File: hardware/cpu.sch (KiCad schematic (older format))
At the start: 76 parts, among them J801 HANDSFREE, J802 microphone, J803 HEADPHONES, P801 TX_SW_WIRE, Q801 Q_PMOS_DGS, SW801 SW_PUSH, SW802 SW, SW803 SW, SW804 SW, SW805 SW, SW806 SW, SW807 SW, SW808 encoder, SW809 encoder, U801 STM32F401, U802 WM8731

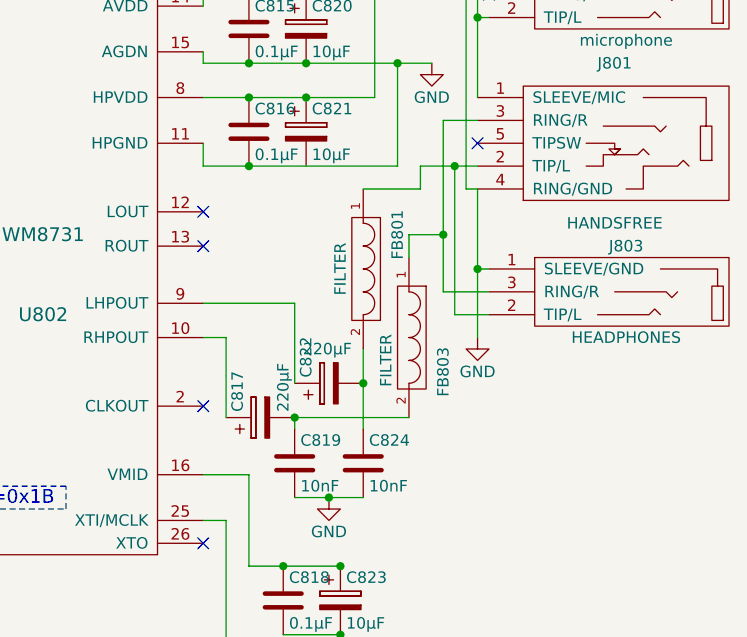
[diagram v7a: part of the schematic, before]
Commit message: fixed some more ERC errors
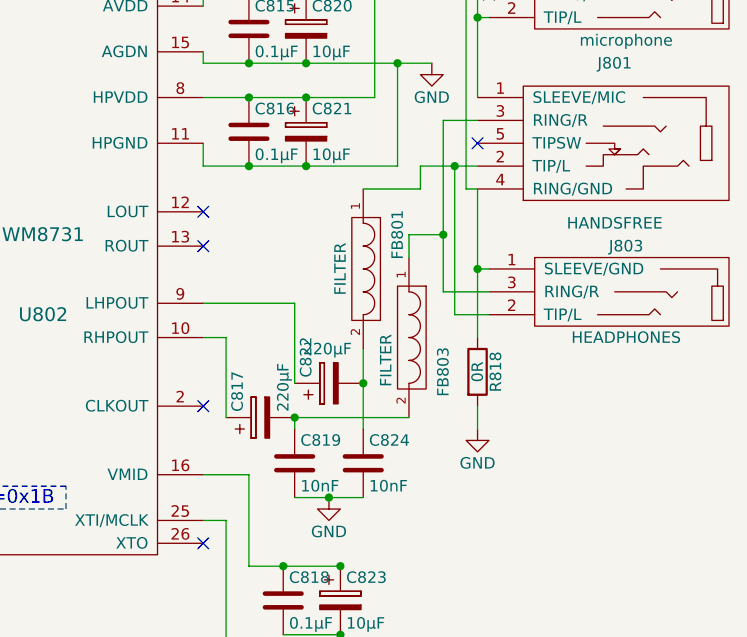
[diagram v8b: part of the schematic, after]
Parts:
- added R818: 0R, symbol R
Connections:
- net GND: now also C821.2, R818.2; no longer J801.4 (RING/GND), J802.1 (SLEEVE/GND), J803.1 (SLEEVE/GND)
- new net: J801.4 (RING/GND), J802.1 (SLEEVE/GND), J803.1 (SLEEVE/GND), R818.1
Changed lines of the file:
@@
 $EndComp
 $Comp
-L +Vlogic #PWR048
+L +Vlogic #PWR053
 U 1 1 57E60A73
 P 1900 1250
-F 0 "#PWR048" H 1900 1050 50  0001 C CNN
+F 0 "#PWR053" H 1900 1050 50  0001 C CNN
 F 1 "+Vlogic" H 1900 1450 50  0000 C CNN
 F 2 "" H 1900 1250 50  0000 C CNN
@@
 $EndComp
 $Comp
-L GND #PWR049
+L GND #PWR054
 U 1 1 57E60AA6
 P 1900 1650
-F 0 "#PWR049" H 1900 1400 50  0001 C CNN
+F 0 "#PWR054" H 1900 1400 50  0001 C CNN
 F 1 "GND" H 1900 1500 50  0000 C CNN
 F 2 "" H 1900 1650 50  0000 C CNN
@@
 $EndComp
 $Comp
-L +Vlogic #PWR050
+L +Vlogic #PWR055
 U 1 1 57E60C30
 P 700 3050
-F 0 "#PWR050" H 700 2850 50  0001 C CNN
+F 0 "#PWR055" H 700 2850 50  0001 C CNN
 F 1 "+Vlogic" H 700 3250 50  0000 C CNN
 F 2 "" H 700 3050 50  0000 C CNN
@@
 $EndComp
 $Comp
-L GND #PWR051
+L GND #PWR056
 U 1 1 57E60C66
 P 850 3000
-F 0 "#PWR051" H 850 2750 50  0001 C CNN
+F 0 "#PWR056" H 850 2750 50  0001 C CNN
 F 1 "GND" H 850 2850 50  0000 C CNN
 F 2 "" H 850 3000 50  0000 C CNN
@@
 $EndComp
 $Comp
-L +Vlogic #PWR052
+L +Vlogic #PWR057
 U 1 1 57E60CF4
 P 5150 1450
-F 0 "#PWR052" H 5150 1250 50  0001 C CNN
+F 0 "#PWR057" H 5150 1250 50  0001 C CNN
 F 1 "+Vlogic" H 5150 1650 50  0000 C CNN
 F 2 "" H 5150 1450 50  0000 C CNN
@@
 $EndComp
 $Comp
-L GND #PWR053
+L GND #PWR058
 U 1 1 57E60D4C
 P 5150 1850
-F 0 "#PWR053" H 5150 1600 50  0001 C CNN
+F 0 "#PWR058" H 5150 1600 50  0001 C CNN
 F 1 "GND" H 5150 1700 50  0000 C CNN
 F 2 "" H 5150 1850 50  0000 C CNN
@@
 $EndComp
 $Comp
-L GND #PWR054
+L GND #PWR059
 U 1 1 57E60E1B
 P 2650 4850
-F 0 "#PWR054" H 2650 4600 50  0001 C CNN
+F 0 "#PWR059" H 2650 4600 50  0001 C CNN
 F 1 "GND" H 2650 4700 50  0000 C CNN
 F 2 "" H 2650 4850 50  0000 C CNN
@@
 $EndComp
 $Comp
-L +Vlogic #PWR055
+L +Vlogic #PWR060
 U 1 1 57E60E3B
 P 3250 4850
-F 0 "#PWR055" H 3250 4650 50  0001 C CNN
+F 0 "#PWR060" H 3250 4650 50  0001 C CNN
 F 1 "+Vlogic" H 3250 5050 50  0000 C CNN
 F 2 "" H 3250 4850 50  0000 C CNN
@@
 $EndComp
 $Comp
-L GND #PWR056
+L GND #PWR061
 U 1 1 57E61093
 P 4900 4450
-F 0 "#PWR056" H 4900 4200 50  0001 C CNN
+F 0 "#PWR061" H 4900 4200 50  0001 C CNN
 F 1 "GND" H 4900 4300 50  0000 C CNN
 F 2 "" H 4900 4450 50  0000 C CNN
@@
 $EndComp
 $Comp
-L +Vlogic #PWR057
+L +Vlogic #PWR062
 U 1 1 57E61099
 P 4900 4050
-F 0 "#PWR057" H 4900 3850 50  0001 C CNN
+F 0 "#PWR062" H 4900 3850 50  0001 C CNN
 F 1 "+Vlogic" H 4900 4250 50  0000 C CNN
 F 2 "" H 4900 4050 50  0000 C CNN
@@
 $EndComp
 $Comp
-L +Vlogic #PWR058
+L +Vlogic #PWR063
 U 1 1 57E633B3
 P 8200 850
-F 0 "#PWR058" H 8200 650 50  0001 C CNN
+F 0 "#PWR063" H 8200 650 50  0001 C CNN
 F 1 "+Vlogic" H 8200 1050 50  0000 C CNN
 F 2 "" H 8200 850 50  0000 C CNN
@@
 $EndComp
 $Comp
-L GND #PWR059
+L GND #PWR064
 U 1 1 57E633EA
 P 6700 1250
-F 0 "#PWR059" H 6700 1000 50  0001 C CNN
+F 0 "#PWR064" H 6700 1000 50  0001 C CNN
 F 1 "GND" H 6700 1100 50  0000 C CNN
 F 2 "" H 6700 1250 50  0000 C CNN
@@
 $EndComp
 $Comp
-L GND #PWR060
+L GND #PWR065
 U 1 1 57E6340F
 P 9900 1300
-F 0 "#PWR060" H 9900 1050 50  0001 C CNN
+F 0 "#PWR065" H 9900 1050 50  0001 C CNN
 F 1 "GND" H 9900 1150 50  0000 C CNN
 F 2 "" H 9900 1300 50  0000 C CNN
@@
 NoConn ~ 8900 3400
 $Comp
-L +Vlogic #PWR061
+L +Vlogic #PWR066
 U 1 1 57E6342B
 P 6550 2900
-F 0 "#PWR061" H 6550 2700 50  0001 C CNN
+F 0 "#PWR066" H 6550 2700 50  0001 C CNN
 F 1 "+Vlogic" H 6550 3100 50  0000 C CNN
 F 2 "" H 6550 2900 50  0000 C CNN
@@
 $EndComp
 $Comp
-L GND #PWR062
+L GND #PWR067
 U 1 1 57E6344F
 P 9500 3800
-F 0 "#PWR062" H 9500 3550 50  0001 C CNN
+F 0 "#PWR067" H 9500 3550 50  0001 C CNN
 F 1 "GND" H 9500 3650 50  0000 C CNN
 F 2 "" H 9500 3800 50  0000 C CNN
@@
 $EndComp
 $Comp
-L GND #PWR063
+L GND #PWR068
 U 1 1 57E63F8E
 P 7400 3850
-F 0 "#PWR063" H 7400 3600 50  0001 C CNN
+F 0 "#PWR068" H 7400 3600 50  0001 C CNN
 F 1 "GND" H 7400 3700 50  0000 C CNN
 F 2 "" H 7400 3850 50  0000 C CNN
@@
 $EndComp
 $Comp
-L GND #PWR064
+L GND #PWR069
 U 1 1 57E6E6D8
 P 9450 3200
-F 0 "#PWR064" H 9450 2950 50  0001 C CNN
+F 0 "#PWR069" H 9450 2950 50  0001 C CNN
 F 1 "GND" H 9450 3050 50  0000 C CNN
 F 2 "" H 9450 3200 50  0000 C CNN
@@
 $EndComp
 $Comp
-L GND #PWR065
+L GND #PWR070
 U 1 1 57E705F5
-P 10100 2500
-F 0 "#PWR065" H 10100 2250 50  0001 C CNN
-F 1 "GND" H 10100 2350 50  0000 C CNN
-F 2 "" H 10100 2500 50  0000 C CNN
-F 3 "" H 10100 2500 50  0000 C CNN
-	1    10100 2500
+P 10100 2900
+F 0 "#PWR070" H 10100 2650 50  0001 C CNN
+F 1 "GND" H 10100 2750 50  0000 C CNN
+F 2 "" H 10100 2900 50  0000 C CNN
+F 3 "" H 10100 2900 50  0000 C CNN
+	1    10100 2900
 	1    0    0    -1
 $EndComp
@@
 $EndComp
 $Comp
-L GND #PWR066
+L GND #PWR071
 U 1 1 57E73E43
 P 6050 2200
-F 0 "#PWR066" H 6050 1950 50  0001 C CNN
+F 0 "#PWR071" H 6050 1950 50  0001 C CNN
 F 1 "GND" H 6050 2050 50  0000 C CNN
 F 2 "" H 6050 2200 50  0000 C CNN
@@
 $EndComp
 $Comp
-L GND #PWR067
+L GND #PWR072
 U 1 1 57E75C81
 P 6450 1050
-F 0 "#PWR067" H 6450 800 50  0001 C CNN
+F 0 "#PWR072" H 6450 800 50  0001 C CNN
 F 1 "GND" H 6450 900 50  0000 C CNN
 F 2 "" H 6450 1050 50  0000 C CNN
@@
 screen backlight
 $Comp
-L +Vlogic #PWR068
+L +Vlogic #PWR073
 U 1 1 57EB8928
 P 1550 4450
-F 0 "#PWR068" H 1550 4250 50  0001 C CNN
+F 0 "#PWR073" H 1550 4250 50  0001 C CNN
 F 1 "+Vlogic" H 1550 4650 50  0000 C CNN
 F 2 "" H 1550 4450 50  0000 C CNN
@@
 $EndComp
 $Comp
-L GND #PWR069
+L GND #PWR074
 U 1 1 57EB8B78
 P 1300 5400
-F 0 "#PWR069" H 1300 5150 50  0001 C CNN
+F 0 "#PWR074" H 1300 5150 50  0001 C CNN
 F 1 "GND" H 1300 5250 50  0000 C CNN
 F 2 "" H 1300 5400 50  0000 C CNN
@@
 $EndComp
 $Comp
-L +Vlogic #PWR070
+L +Vlogic #PWR075
 U 1 1 57EC1B18
 P 700 3500
-F 0 "#PWR070" H 700 3300 50  0001 C CNN
+F 0 "#PWR075" H 700 3300 50  0001 C CNN
 F 1 "+Vlogic" H 700 3700 50  0000 C CNN
 F 2 "" H 700 3500 50  0000 C CNN
@@
 $EndComp
 $Comp
-L GND #PWR071
+L GND #PWR076
 U 1 1 57EC26E5
 P 1100 4200
-F 0 "#PWR071" H 1100 3950 50  0001 C CNN
+F 0 "#PWR076" H 1100 3950 50  0001 C CNN
 F 1 "GND" H 1100 4050 50  0000 C CNN
 F 2 "" H 1100 4200 50  0000 C CNN
@@
 NoConn ~ 3200 2100
 $Comp
-L GND #PWR072
+L GND #PWR077
 U 1 1 57ED45C9
 P 650 2550
-F 0 "#PWR072" H 650 2300 50  0001 C CNN
+F 0 "#PWR077" H 650 2300 50  0001 C CNN
 F 1 "GND" H 650 2400 50  0000 C CNN
 F 2 "" H 650 2550 50  0000 C CNN
@@
 $EndComp
 $Comp
-L +Vlogic #PWR073
+L +Vlogic #PWR078
 U 1 1 57ED529A
 P 650 800
-F 0 "#PWR073" H 650 600 50  0001 C CNN
+F 0 "#PWR078" H 650 600 50  0001 C CNN
 F 1 "+Vlogic" H 650 1000 50  0000 C CNN
 F 2 "" H 650 800 50  0000 C CNN
@@
 	1    0    0    -1
 $EndComp
+Connection ~ 9350 1750
+$Comp
+L R R818
+U 1 1 57EE56EA
+P 10100 2650
+F 0 "R818" V 10180 2650 50  0000 C CNN
+F 1 "0R" V 10100 2650 50  0000 C CNN
+F 2 "" V 10030 2650 50  0000 C CNN
+F 3 "" H 10100 2650 50  0000 C CNN
+	1    10100 2650
+	1    0    0    -1
+$EndComp
+Wire Wire Line
+	10100 2800 10100 2900
 $EndSCHEMATC
